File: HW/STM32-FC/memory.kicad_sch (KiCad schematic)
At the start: 9 parts, among them J4 Micro_SD_Card_Det1, U5 W25X40CLSN

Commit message: 2025.02.06 PCB routing done v2
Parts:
- C19, C20: LCSC (none) -> C1581
- J4: LCSC (none) -> C719027
- R11, R12, R13, R14, R15: LCSC (none) -> C25531
- U5: LCSC (none) -> C19617
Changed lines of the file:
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@@
+			)
+		)
+		(property "LCSC" "C25531"
+			(at 142.24 29.21 0)
+			(effects
+				(font
+					(size 1.27 1.27)
+				)
+				(hide yes)
 			)
 		)
@@
 		)
 		(property "Sim.Pins" ""
+			(at 146.05 55.88 0)
+			(effects
+				(font
+					(size 1.27 1.27)
+				)
+				(hide yes)
+			)
+		)
+		(property "LCSC" "C25531"
 			(at 146.05 55.88 0)
 			(effects
@@
 			)
 		)
+		(property "LCSC" "C25531"
+			(at 139.7 29.21 0)
+			(effects
+				(font
+					(size 1.27 1.27)
+				)
+				(hide yes)
+			)
+		)
 		(pin "1"
 		)
@@
 		)
 		(property "Sim.Pins" ""
+			(at 137.16 29.21 0)
+			(effects
+				(font
+					(size 1.27 1.27)
+				)
+				(hide yes)
+			)
+		)
+		(property "LCSC" "C25531"
 			(at 137.16 29.21 0)
 			(effects
@@
 		)
 		(property "Sim.Pins" ""
+			(at 175.26 43.18 0)
+			(effects
+				(font
+					(size 1.27 1.27)
+				)
+				(hide yes)
+			)
+		)
+		(property "LCSC" "C719027"
 			(at 175.26 43.18 0)
 			(effects
@@
 			)
 		)
+		(property "LCSC" "C1581"
+			(at 53.34 48.26 0)
+			(effects
+				(font
+					(size 1.27 1.27)
+				)
+				(hide yes)
+			)
+		)
 		(pin "1"
 		)
@@
 			)
 		)
+		(property "LCSC" "C1581"
+			(at 107.95 44.45 0)
+			(effects
+				(font
+					(size 1.27 1.27)
+				)
+				(hide yes)
+			)
+		)
 		(pin "1"
 		)
@@
 		)
 		(property "Sim.Pins" ""
+			(at 144.78 29.21 0)
+			(effects
+				(font
+					(size 1.27 1.27)
+				)
+				(hide yes)
+			)
+		)
+		(property "LCSC" "C25531"
 			(at 144.78 29.21 0)
 			(effects
@@
 			(at 80.01 36.83 0)
 			(effects
+				(font
+					(size 1.27 1.27)
+				)
+				(hide yes)
+			)
+		)
+		(property "LCSC" "C19617"
+			(at 80.01 36.83 0)
+			(effects

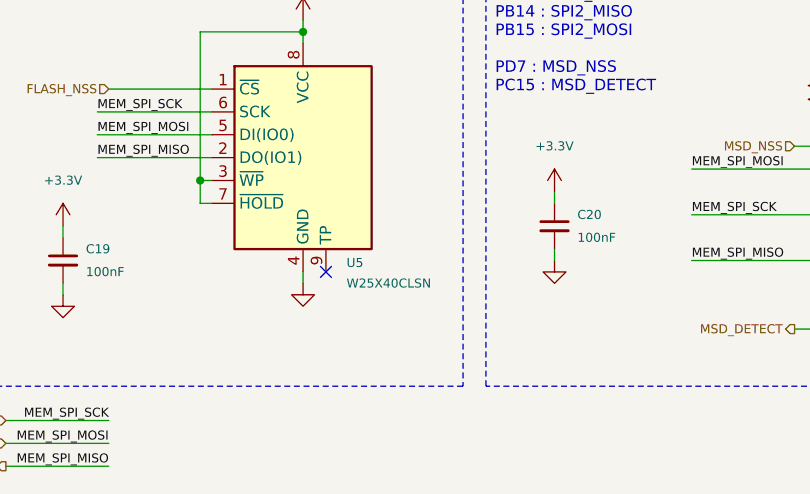
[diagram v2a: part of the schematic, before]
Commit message: 2025.02.07 USB C Conn change v1
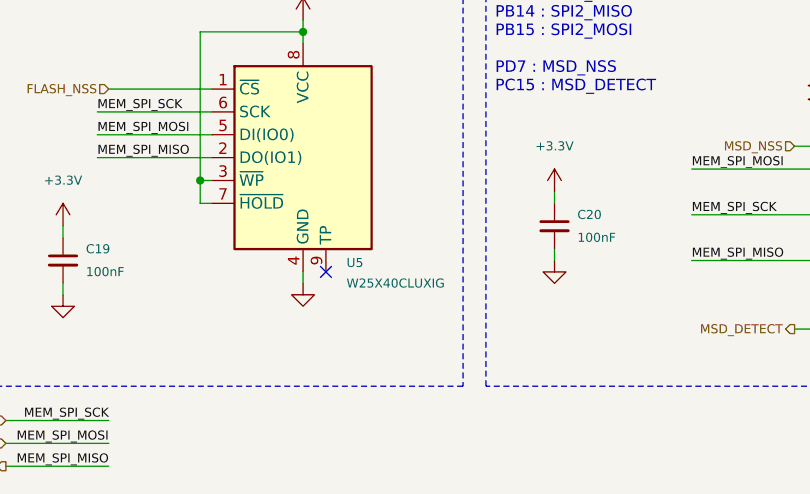
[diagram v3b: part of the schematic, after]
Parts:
- C19, C20: LCSC C1581 -> C1525
- U5: value W25X40CLSN -> W25X40CLUXIG; LCSC C19617 -> C401661
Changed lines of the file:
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@@
 			)
 		)
-		(property "LCSC" "C1581"
+		(property "LCSC" "C1525"
 			(at 53.34 48.26 0)
 			(effects
@@
 			)
 		)
-		(property "LCSC" "C1581"
+		(property "LCSC" "C1525"
 			(at 107.95 44.45 0)
 			(effects
@@
 			)
 		)
-		(property "Value" "W25X40CLSN"
+		(property "Value" "W25X40CLUXIG"
 			(at 84.836 50.8 0)
 			(effects
@@
 			)
 		)
-		(property "LCSC" "C19617"
-			(at 80.01 36.83 0)
-			(effects
+		(property "LCSC" "C401661"
+			(at 80.01 36.83 0)
+			(effects

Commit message: 2025.02.11 PCB DONE! MEMO UPDATING
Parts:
- removed J4: Micro_SD_Card_Det1, Connector_Card:microSD_HC_Hirose_DM3D-SF, symbol Connector:Micro_SD_Card_Det1
- added J4: TF-06A, TF06A, symbol TF-06A:TF-06A
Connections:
- net +3.3V: now also J4.4 (VDD)
- net GND: now also J4.6 (VSS), J4.MP1, J4.MP2, J4.MP3, J4.MP4
- net MEM_SPI_MISO: now also J4.7 (DO)
- net MEM_SPI_MOSI: now also J4.3 (DI)
- net MEM_SPI_SCK: now also J4.5 (SCLK)
- net MSD_NSS: now also J4.2 (CS)
- net at R15.2: now also J4.G1 (SWICTH)
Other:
- note added: "SPI2_SCK : PB13 SPI2_MISO : PB14 SPI2_MOSI : PB15 FLASH_NSS : PC13"
- note added: "SPI2_SCK : PB13 SPI2_MISO : PB14 SPI2_MOSI : PB15 MSD_NSS : PD7 MSD_DETECT : PC15"
- note removed: "PB13 : SPI2_SCK PB14 : SPI2_MISO PB15 : SPI2_MOSI PC13 : FLASH_NSS"
- note removed: "PB13 : SPI2_SCK PB14 : SPI2_MISO PB15 : SPI2_MOSI PD7 : MSD_NSS PC15 : MSD_DETECT"
- moved on the sheet: R11, R12, R13, R14, R15

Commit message: Test software v1
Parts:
- renumbered C19 to C20, C20 to C21, R11 to R12, R12 to R13, R13 to R14, R14 to R15, R15 to R16
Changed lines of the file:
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@@
 	(title_block
 		(title "Memory")
-		(date "2025-02-08")
+		(date "2025-02-23")
 		(rev "A")
 		(company "NARAE")
@@
 		(on_board yes)
 		(dnp no)
-		(property "Reference" "R13"
+		(property "Reference" "R14"
 			(at 139.7 31.242 90)
 			(effects
@@
 			(project "STM32-FC"
 				(path "/8d4cc317-3933-4aa6-844b-8c5c635e89c7/3e7c6c79-bc31-4cc9-af6a-d0a28245a7b2"
-					(reference "R13")
+					(reference "R14")
 					(unit 1)
 				)
@@
 		(dnp no)
 		(fields_autoplaced yes)
-		(property "Reference" "#PWR042"
+		(property "Reference" "#PWR043"
 			(at 53.34 48.26 0)
 			(effects
@@
 			(project ""
 				(path "/8d4cc317-3933-4aa6-844b-8c5c635e89c7/3e7c6c79-bc31-4cc9-af6a-d0a28245a7b2"
-					(reference "#PWR042")
+					(reference "#PWR043")
 					(unit 1)
 				)
@@
 		(on_board yes)
 		(dnp no)
-		(property "Reference" "R15"
+		(property "Reference" "R16"
 			(at 190.246 34.29 90)
 			(effects
@@
 			(project "STM32-FC"
 				(path "/8d4cc317-3933-4aa6-844b-8c5c635e89c7/3e7c6c79-bc31-4cc9-af6a-d0a28245a7b2"
-					(reference "R15")
+					(reference "R16")
 					(unit 1)
 				)
@@
 		(dnp no)
 		(fields_autoplaced yes)
-		(property "Reference" "#PWR047"
+		(property "Reference" "#PWR048"
 			(at 107.95 54.61 0)
 			(effects
@@
 			(project ""
 				(path "/8d4cc317-3933-4aa6-844b-8c5c635e89c7/3e7c6c79-bc31-4cc9-af6a-d0a28245a7b2"
-					(reference "#PWR047")
+					(reference "#PWR048")
 					(unit 1)
 				)
@@
 		(dnp no)
 		(fields_autoplaced yes)
-		(property "Reference" "#PWR043"
+		(property "Reference" "#PWR044"
 			(at 53.34 58.42 0)
 			(effects
@@
 			(project ""
 				(path "/8d4cc317-3933-4aa6-844b-8c5c635e89c7/3e7c6c79-bc31-4cc9-af6a-d0a28245a7b2"
-					(reference "#PWR043")
+					(reference "#PWR044")
 					(unit 1)
 				)
@@
 		(dnp no)
 		(fields_autoplaced yes)
-		(property "Reference" "#PWR050"
+		(property "Reference" "#PWR051"
 			(at 190.5 45.72 0)
 			(effects
@@
 			(project "STM32-FC"
 				(path "/8d4cc317-3933-4aa6-844b-8c5c635e89c7/3e7c6c79-bc31-4cc9-af6a-d0a28245a7b2"
-					(reference "#PWR050")
+					(reference "#PWR051")
 					(unit 1)
 				)
@@
 		(on_board yes)
 		(dnp no)
-		(property "Reference" "R12"
+		(property "Reference" "R13"
 			(at 137.16 31.242 90)
 			(effects
@@
 			(project "STM32-FC"
 				(path "/8d4cc317-3933-4aa6-844b-8c5c635e89c7/3e7c6c79-bc31-4cc9-af6a-d0a28245a7b2"
-					(reference "R12")
+					(reference "R13")
 					(unit 1)
 				)
@@
 		(on_board yes)
 		(dnp no)
-		(property "Reference" "R11"
+		(property "Reference" "R12"
 			(at 134.62 31.242 90)
 			(effects
@@
 			(project "STM32-FC"
 				(path "/8d4cc317-3933-4aa6-844b-8c5c635e89c7/3e7c6c79-bc31-4cc9-af6a-d0a28245a7b2"
-					(reference "R11")
+					(reference "R12")
 					(unit 1)
 				)
@@
 		(dnp no)
 		(fields_autoplaced yes)
-		(property "Reference" "#PWR044"
+		(property "Reference" "#PWR045"
 			(at 80.01 25.4 0)
 			(effects
@@
 			(project ""
 				(path "/8d4cc317-3933-4aa6-844b-8c5c635e89c7/3e7c6c79-bc31-4cc9-af6a-d0a28245a7b2"
-					(reference "#PWR044")
+					(reference "#PWR045")
 					(unit 1)
 				)
@@
 		(dnp no)
 		(fields_autoplaced yes)
-		(property "Reference" "#PWR049"
+		(property "Reference" "#PWR050"
 			(at 135.89 45.72 0)
 			(effects
@@
 			(project "STM32-FC"
 				(path "/8d4cc317-3933-4aa6-844b-8c5c635e89c7/3e7c6c79-bc31-4cc9-af6a-d0a28245a7b2"
-					(reference "#PWR049")
+					(reference "#PWR050")
 					(unit 1)
 				)
@@
 		(on_board yes)
 		(dnp no)
-		(property "Reference" "C19"
+		(property "Reference" "C20"
 			(at 55.88 46.99 0)
 			(effects
@@
 			(project "STM32-FC"
 				(path "/8d4cc317-3933-4aa6-844b-8c5c635e89c7/3e7c6c79-bc31-4cc9-af6a-d0a28245a7b2"
-					(reference "C19")
+					(reference "C20")
 					(unit 1)
 				)
@@
 		(on_board yes)
 		(dnp no)
-		(property "Reference" "C20"
+		(property "Reference" "C21"
 			(at 110.49 43.18 0)
 			(effects
@@
 			(project "STM32-FC"
 				(path "/8d4cc317-3933-4aa6-844b-8c5c635e89c7/3e7c6c79-bc31-4cc9-af6a-d0a28245a7b2"
-					(reference "C20")
+					(reference "C21")
 					(unit 1)
 				)
@@
 		(on_board yes)
 		(dnp no)
-		(property "Reference" "R14"
+		(property "Reference" "R15"
 			(at 142.24 31.242 90)
 			(effects
@@
 			(project "STM32-FC"
 				(path "/8d4cc317-3933-4aa6-844b-8c5c635e89c7/3e7c6c79-bc31-4cc9-af6a-d0a28245a7b2"
-					(reference "R14")
+					(reference "R15")
 					(unit 1)
 				)
@@
 		(dnp no)
 		(fields_autoplaced yes)
-		(property "Reference" "#PWR046"
+		(property "Reference" "#PWR047"
 			(at 107.95 44.45 0)
 			(effects
@@
 			(project ""
 				(path "/8d4cc317-3933-4aa6-844b-8c5c635e89c7/3e7c6c79-bc31-4cc9-af6a-d0a28245a7b2"
-					(reference "#PWR046")
+					(reference "#PWR047")
 					(unit 1)
 				)
@@
 		(dnp no)
 		(fields_autoplaced yes)
-		(property "Reference" "#PWR045"
+		(property "Reference" "#PWR046"
 			(at 80.01 57.15 0)
 			(effects
@@
 			(project ""
 				(path "/8d4cc317-3933-4aa6-844b-8c5c635e89c7/3e7c6c79-bc31-4cc9-af6a-d0a28245a7b2"
-					(reference "#PWR045")
+					(reference "#PWR046")
 					(unit 1)
 				)
@@
 		(on_board yes)
 		(dnp no)
-		(property "Reference" "#PWR048"
+		(property "Reference" "#PWR049"
 			(at 133.35 25.4 0)
 			(effects
@@
 			(project "STM32-FC"
 				(path "/8d4cc317-3933-4aa6-844b-8c5c635e89c7/3e7c6c79-bc31-4cc9-af6a-d0a28245a7b2"
-					(reference "#PWR048")
+					(reference "#PWR049")
 					(unit 1)
 				)
